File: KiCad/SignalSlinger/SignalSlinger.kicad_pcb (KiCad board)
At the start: 2 copper layers, 92.1 x 59.1 mm, 106 parts, among them J101 Conn_01x02, J102 Conn_01x03, J103 Conn_01x02, J104 Conn_01x02, J105 Conn_01x04, J106 Conn_01x02, J107 DB9 Female, J108 Conn_01x02, J109 Conn_01x03, J201 Barrel_Jack_Switch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

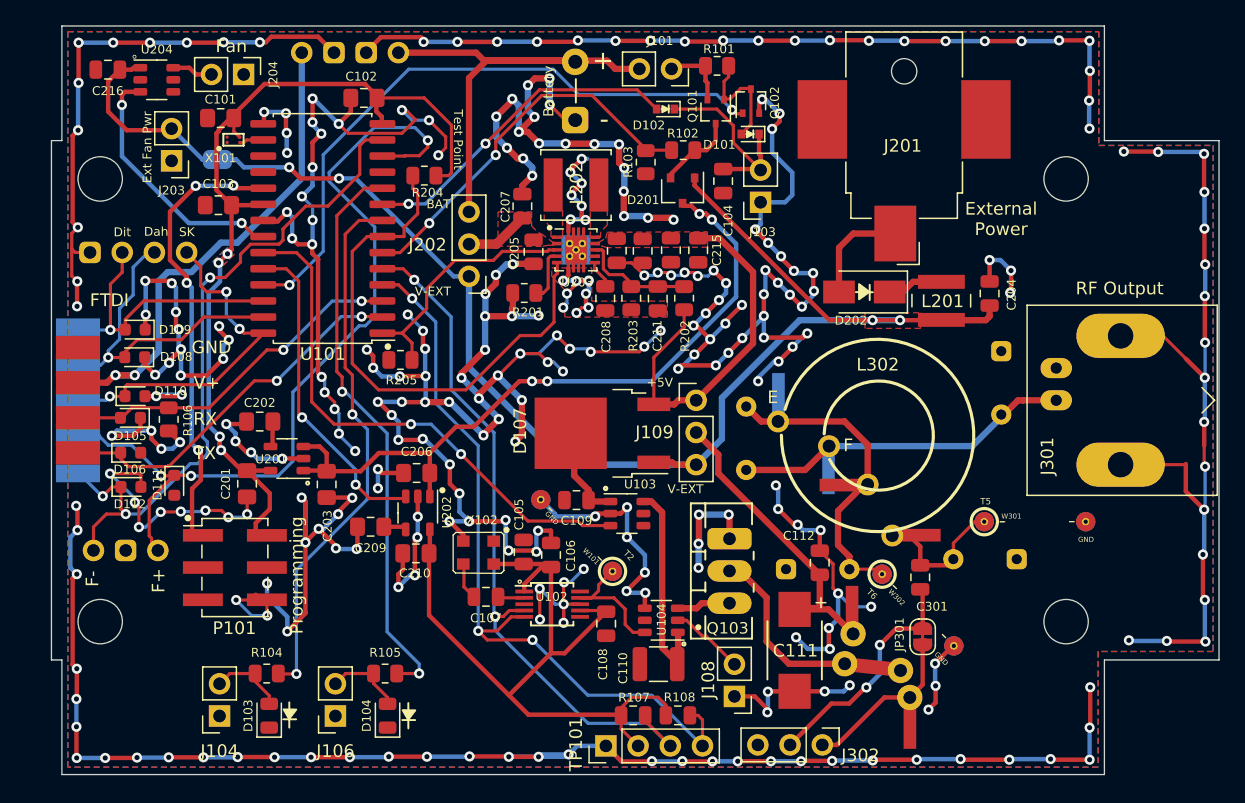
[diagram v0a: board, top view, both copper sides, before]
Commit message: Schematic Updates
o Added support for a linear adjustable voltage regulator
o Added a switch
o Re-arranged components for a better fit
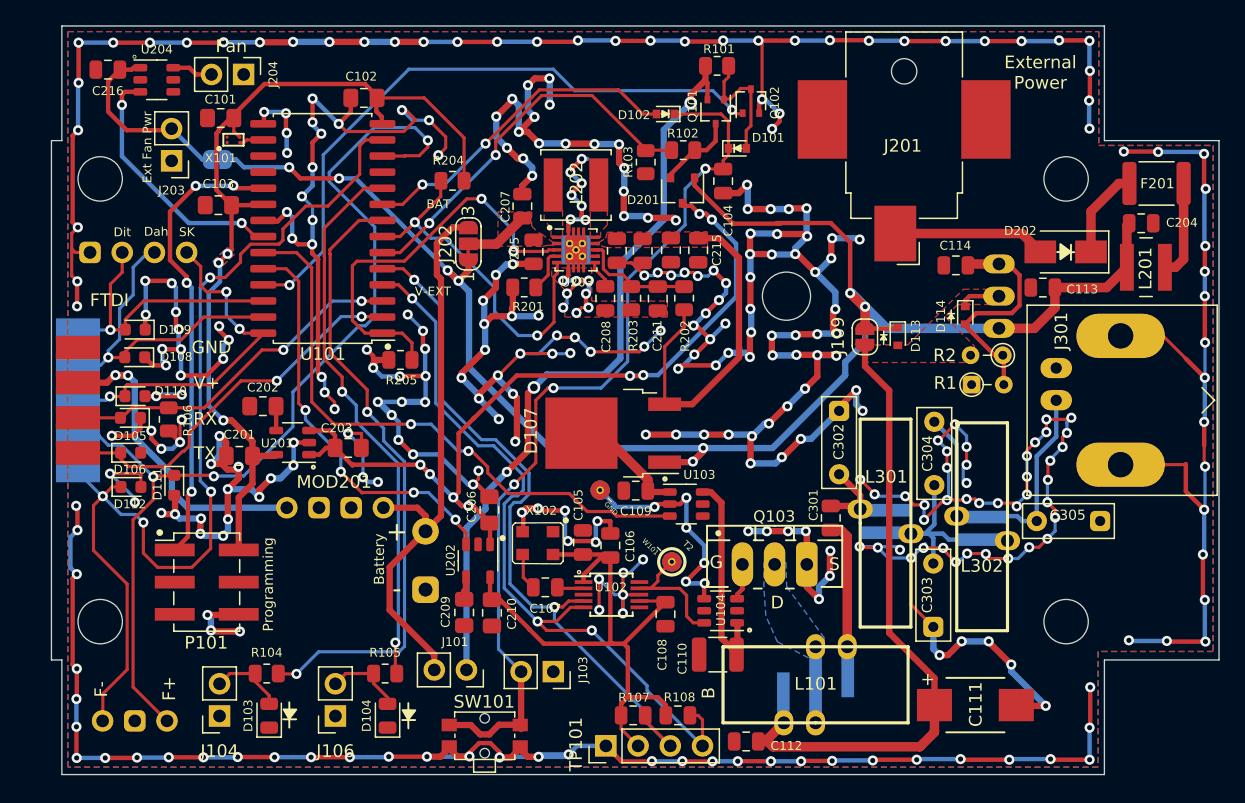
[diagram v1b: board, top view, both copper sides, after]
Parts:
- removed J108: Conn_01x02, Connector_PinHeader_2.54mm:PinHeader_1x02_P2.54mm_Vertical
- removed J302: Conn_01x03, Connector_PinHeader_2.54mm:PinHeader_1x03_P2.54mm_Vertical
- removed JP301: QRP disable, Jumper:SolderJumper-2_P1.3mm_Bridged_RoundedPad1.0x1.5mm
- removed W301: T5, Measurement:Measurement_Point_ScopeProbe_Round-SMD-2sides-Pad_Small
- removed W302: T6, Measurement:Measurement_Point_ScopeProbe_Round-SMD-2sides-Pad_Small
- added C113: 10uF, Capacitor_SMD:C_0805_2012Metric, F.Cu at (126.2, 80.5)
- added C114: 10uF, Capacitor_SMD:C_0805_2012Metric, F.Cu at (119.4, 78.8)
- added D113: 1N914WT, Diode_SMD:D_SOD-523, F.Cu at (114.8, 84.4)
- added D114: 1N914WT, Diode_SMD:D_SOD-523, F.Cu at (120.1, 82.7)
- added F201: 1.1A, Fuse:Fuse_1812_4532Metric, F.Cu at (135.2, 72.3)
- added R1: TBD, Resistor_THT:R_Axial_DIN0204_L3.6mm_D1.6mm_P2.54mm_Vertical, F.Cu at (120.6, 88.2)
- added R2: TBD, Resistor_THT:R_Axial_DIN0204_L3.6mm_D1.6mm_P2.54mm_Vertical, F.Cu at (123.1, 85.9)
- added SW101: SW_SPST, Button_Switch_SMD:SW_SPST_TL1014BF160QG, F.Cu at (82.2, 115.9)
- added U105: LT1086-ADJ, TO_SOT_Packages:TO-220_Neutral123_Horizontal, B.Cu at (122.8, 81.2)
- C302, C303, C304, C305: moved to F.Cu
- J109: value Conn_01x03 -> SolderJumper_2_Bridged; footprint Connector_PinHeader_2.54mm:PinHeader_1x03_P2.54mm_Vertical -> Jumper:SolderJumper-2_P1.3mm_Bridged_RoundedPad1.0x1.5mm
- J202: value Conn_01x03 -> SolderJumper_3_Bridged12; footprint Connector_PinHeader_2.54mm:PinHeader_1x03_P2.54mm_Vertical -> Jumper:SolderJumper-3_P1.3mm_Bridged12_RoundedPad1.0x1.5mm_NumberLabels
- L101: footprint Inductors:Toroid_T-50A_TH_BF_CT -> Inductors:Toroid_T-50A_TH_BF_CT_Vertical; moved to F.Cu
- L301: footprint Inductors:Toroid_T-60_2TH -> Inductors:Toroid_T-60_2TH_Vertical; moved to F.Cu
- L302: footprint Inductors:Toroid_T-60_2TH -> Inductors:Toroid_T-60_2TH_Vertical
- R105: value 1k -> 220
- R203: value 105k -> 80.6k
- moved J101 50.1 mm to (80.8, 110.7)
- moved J103 40.5 mm to (87.6, 110.8), turned to -90 degrees
- moved BT201 38.9 mm to (77.5, 99.8)
- moved MOD201 35.9 mm to (74.2, 97.9)
- moved L201 16.4 mm to (134.3, 78.9), turned to 180 degrees
- moved D202 16.2 mm to (128.0, 77.7)
- moved C304 15.3 mm to (117.7, 91.1), turned to -90 degrees
- moved C112 15.2 mm to (102.8, 116.3), turned to 0 degrees
- moved C111 14.9 mm to (120.9, 113.5), turned to 0 degrees
- moved J109 14.2 mm to (112.2, 84.4), turned to -90 degrees
- moved J102 13.5 mm to (52.0, 114.7)
- moved C204 13.2 mm to (134.0, 75.5), turned to 180 degrees
- moved C303 12.5 mm to (117.6, 107.3), turned to 90 degrees
- moved C302 11.2 mm to (110.2, 95.2), turned to 90 degrees
- moved L302 10.9 mm to (121.4, 99.4), turned to 180 degrees
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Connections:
- C112 pad 1: Net-(C111-Pad1) -> GND
- C112 pad 2: GND -> Net-(C111-Pad1)
- C212 pad 1: +5V -> +7V
- C213 pad 2: +5V -> +7V
- C214 pad 2: +5V -> +7V
- C215 pad 2: +5V -> +7V
- C301 pad 1: Net-(C301-Pad1) -> RF_Raw
- D107 pad 3: +5V -> +7V
- J109 pad 1: +5V -> V_ext
- L201 pad 1: Net-(D202-Pad1) -> Net-(L201-Pad1)
- R202 pad 1: +5V -> +7V
- U104 pad 2: Net-(J108-Pad2) -> unconnected-(U104-Pad2)
- U203 pad 9: +5V -> +7V
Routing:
- net GND: track 796.1 -> 863.4 mm, vias 306 -> 353
- net Net-(J101-Pad1): track 5.11 -> 59.7 mm, vias 0 -> 3
- net Net-(C104-Pad1): track 15.4 -> 69.9 mm, vias 0 -> 3
- net +5V: track 29.3 -> 0.00 mm
- net Net-(C111-Pad1): track 25.1 -> 52.6 mm
- net V_ext: track 106.9 -> 134.3 mm, vias 4 -> 8
- net +7V: track 0.00 -> 27.2 mm
- net Frequency Down: track 54.6 -> 79.6 mm, vias 3 -> 4
- net Net-(C301-Pad1): track 18.5 -> 0.00 mm, vias 2 -> 0
- net Net-(R1-Pad2): track 0.00 -> 17.0 mm
- net Power_Good: track 42.9 -> 28.4 mm, vias 0 -> 2
- net V+_Charging: track 40.6 -> 26.5 mm
- net Net-(L101-Pad2): track 13.3 -> 0.00 mm
- net Frequency Up: track 66.4 -> 79.6 mm
- net B/B_PS_Enable: track 19.6 -> 31.9 mm, vias 0 -> 2
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- added copper zone on F.Cu, net +7V
- added copper zone on F.Cu, net Net-(C111-Pad1)
- added copper zone on B.Cu, net Net-(L101-Pad2)
- removed copper zone on F.Cu, net +5V
- removed copper zone on F.Cu, net V_ext
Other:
- board text added: "SignalSlinger github.com/OpenARDF/SignalSlinger Open Source: MIT License Model: SS-80/40 Nov 2023"
- board text removed: "+5V"
- board text removed: "Adafruit LiIon Charging Module PID_1904"
- board text removed: "Foxoring Module"
- board text removed: "SignalSlinger github.com/OpenARDF/SignalSlinger Open Source: MIT License Model: SS-80/40 July 2023"
- board text removed: "Test Point"

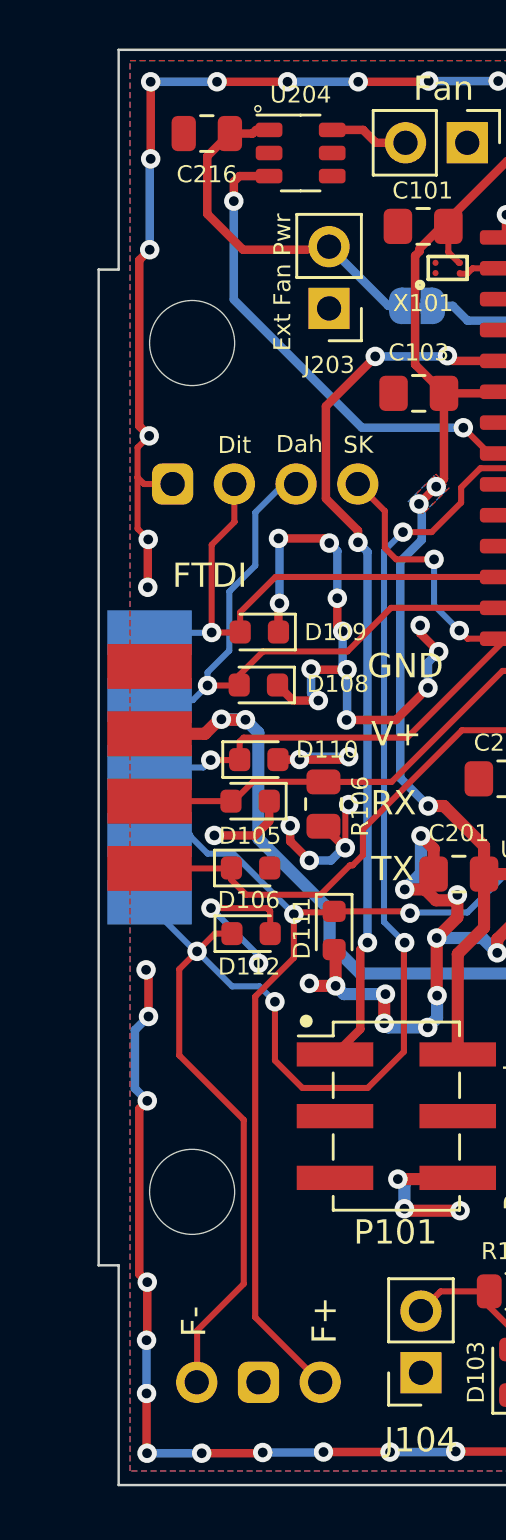
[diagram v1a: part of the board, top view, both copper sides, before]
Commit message: PCB Updates
Moved DB9 2mm farther left, and extended PCB to match.
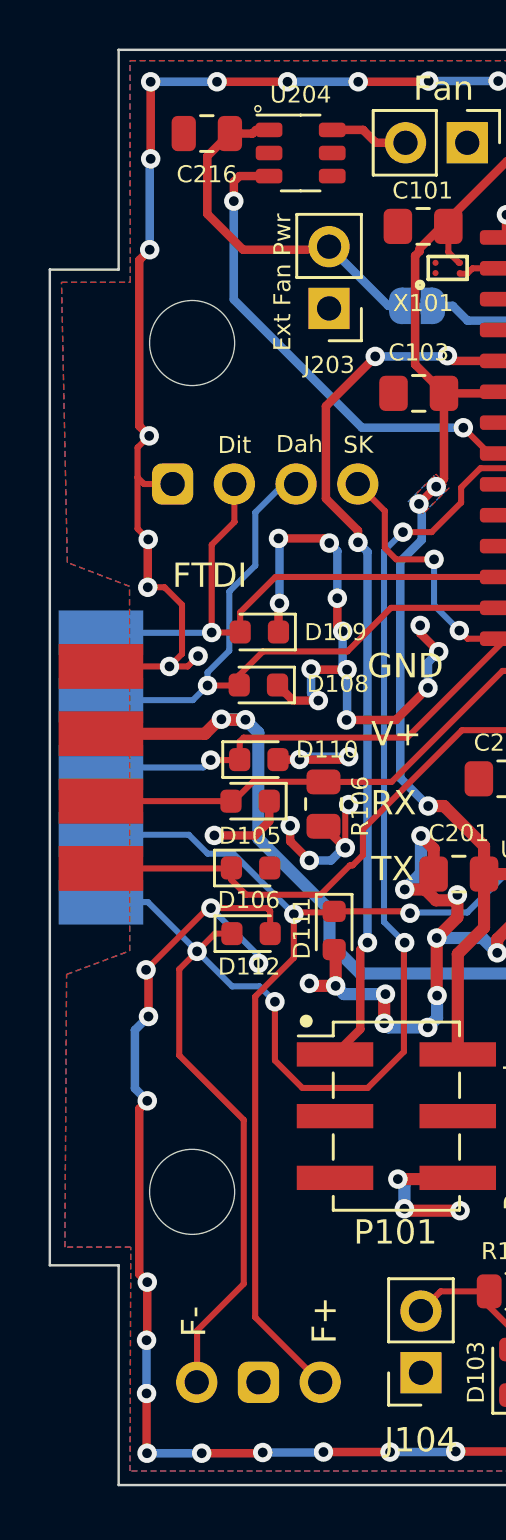
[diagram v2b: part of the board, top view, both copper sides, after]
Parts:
- moved J107 2.00 mm to (48.1, 89.4)
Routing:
- net GND: track 863.4 -> 875.7 mm, vias 353 -> 355
- net Frequency Down: track 79.6 -> 81.7 mm
- net Frequency Up: track 79.6 -> 81.6 mm
- net V+_Charging: track 26.5 -> 28.4 mm
- net Straightkey: track 27.8 -> 29.7 mm
- net Paddle_Dit: track 22.4 -> 24.3 mm
- net Paddle Dah: track 26.0 -> 27.9 mm
- net Net-(D106-Pad1): track 30.1 -> 32.0 mm
- net Net-(D105-Pad2): track 27.8 -> 29.7 mm
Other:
- board size 92.1 x 59.1 mm -> 94.1 x 59.1 mm

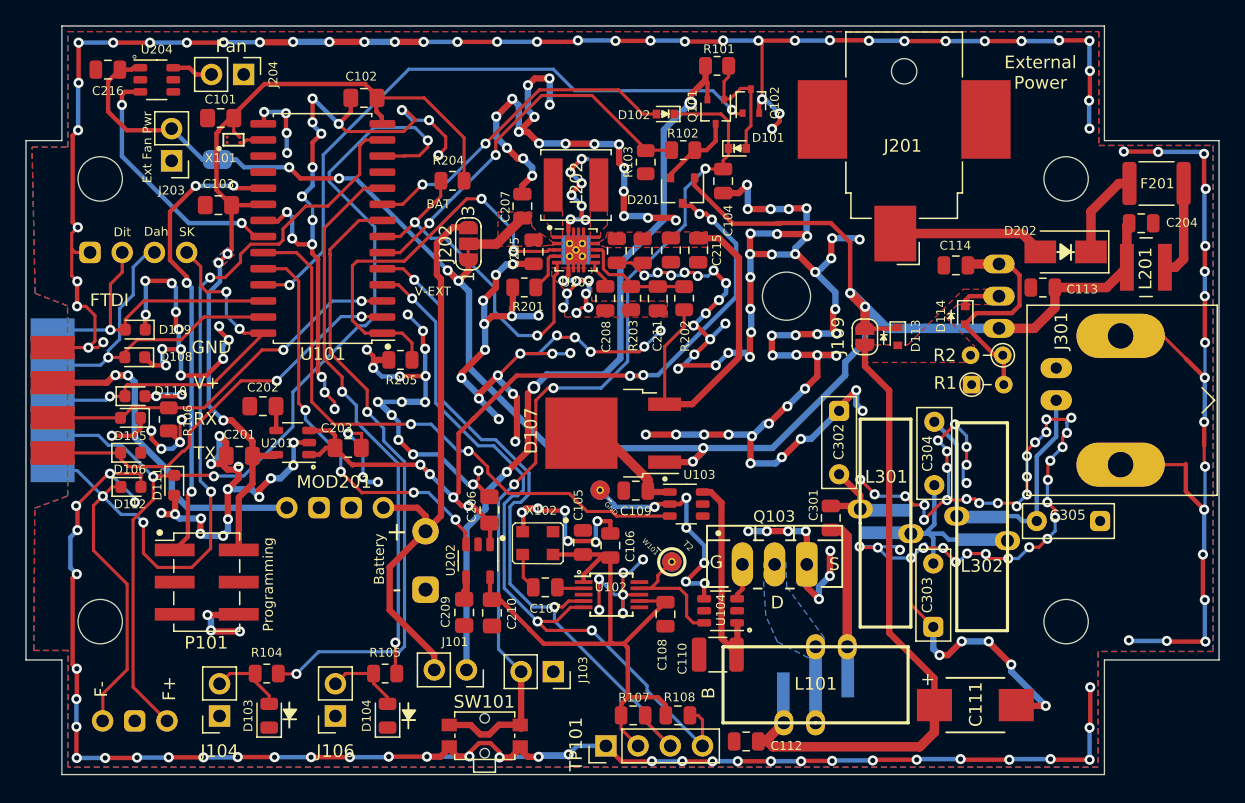
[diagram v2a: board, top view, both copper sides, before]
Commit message: DB9 Pinout Updates
o Updated schematic (Rev 2.0)
o Updated PCB
o Updated Gerbers
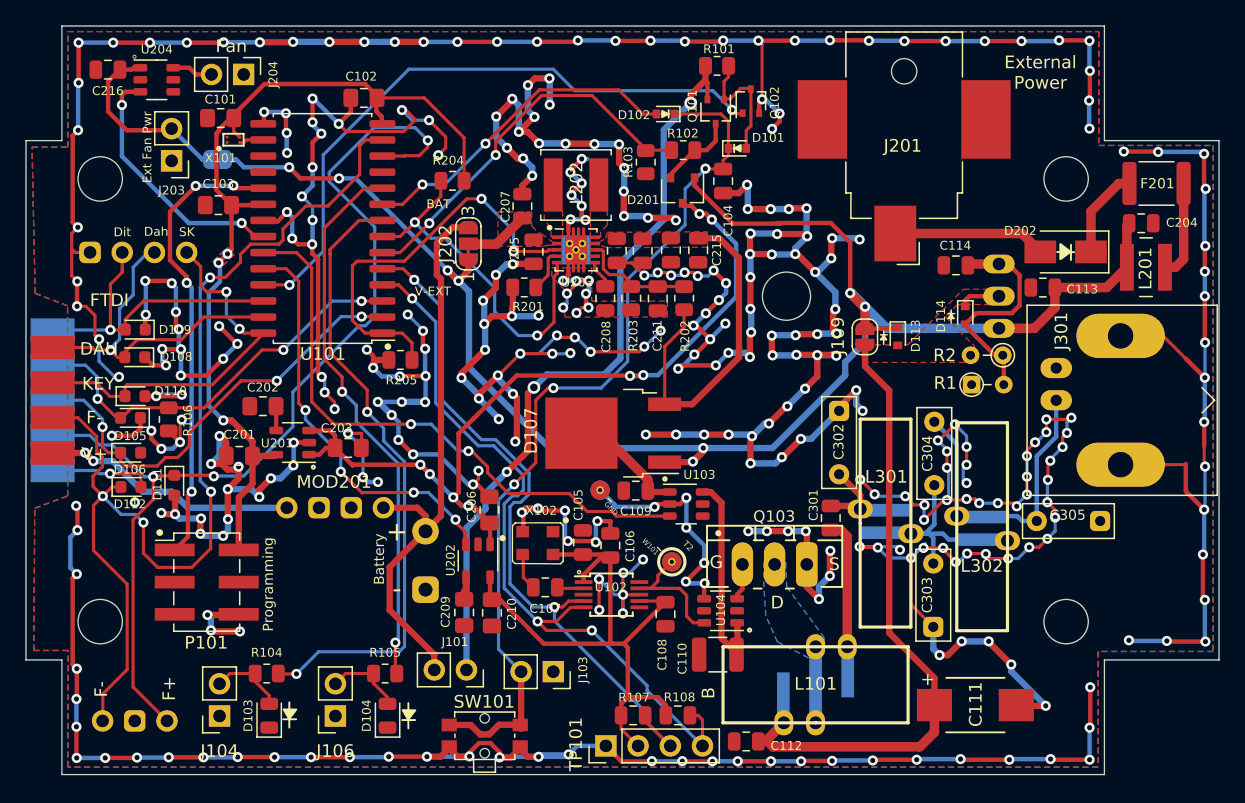
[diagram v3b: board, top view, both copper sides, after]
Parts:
- U105: value LT1086-ADJ -> TO-220 ADJ Reg.
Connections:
- D105 pad 2: Net-(D105-Pad2) -> Net-(J107-Pad2)
- D106 pad 1: Net-(D106-Pad1) -> Net-(J107-Pad3)
- J107 pad 2: Paddle Dah -> Net-(J107-Pad2)
- J107 pad 3: Straightkey -> Net-(J107-Pad3)
- J107 pad 5: Frequency Down -> GND
- J107 pad 6: GND -> Paddle Dah
- J107 pad 7: V+_Charging -> Straightkey
- J107 pad 8: Net-(D105-Pad2) -> Frequency Down
- J107 pad 9: Net-(D106-Pad1) -> V+_Charging
- R106 pad 1: Net-(D105-Pad2) -> Net-(J107-Pad2)
- U101 pad 2: Net-(D106-Pad1) -> Net-(J107-Pad3)
- U101 pad 3: Net-(D105-Pad2) -> Net-(J107-Pad2)
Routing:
- net Net-(J107-Pad3): track 0.00 -> 35.3 mm, vias 0 -> 3
- net Net-(J107-Pad2): track 0.00 -> 32.4 mm, vias 0 -> 3
- net Net-(D106-Pad1): track 32.0 -> 0.00 mm, vias 2 -> 0
- net Net-(D105-Pad2): track 29.7 -> 0.00 mm, vias 2 -> 0
- net V+_Charging: track 28.4 -> 21.2 mm
- net Frequency Down: track 81.7 -> 86.5 mm
- net GND: track 875.7 -> 873.4 mm
- net Paddle Dah: track 27.9 -> 27.3 mm
- net Straightkey: track 29.7 -> 30.0 mm, vias 3 -> 2
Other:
- board text added: "RXD"
- board text added: "SignalSlinger github.com/OpenARDF/SignalSlinger Open Source: MIT License Model: SS-80 Nov 2023"
- board text added: "TXD"
- board text removed: "FREQ+"
- board text removed: "FREQ-"
- board text removed: "RX"
- board text removed: "SignalSlinger github.com/OpenARDF/SignalSlinger Open Source: MIT License Model: SS-80/40 Nov 2023"
- board text removed: "TX"

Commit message: Updates
PCB and FreeCAD file updates. PCB layout improved to ensure all parts fit without interference.
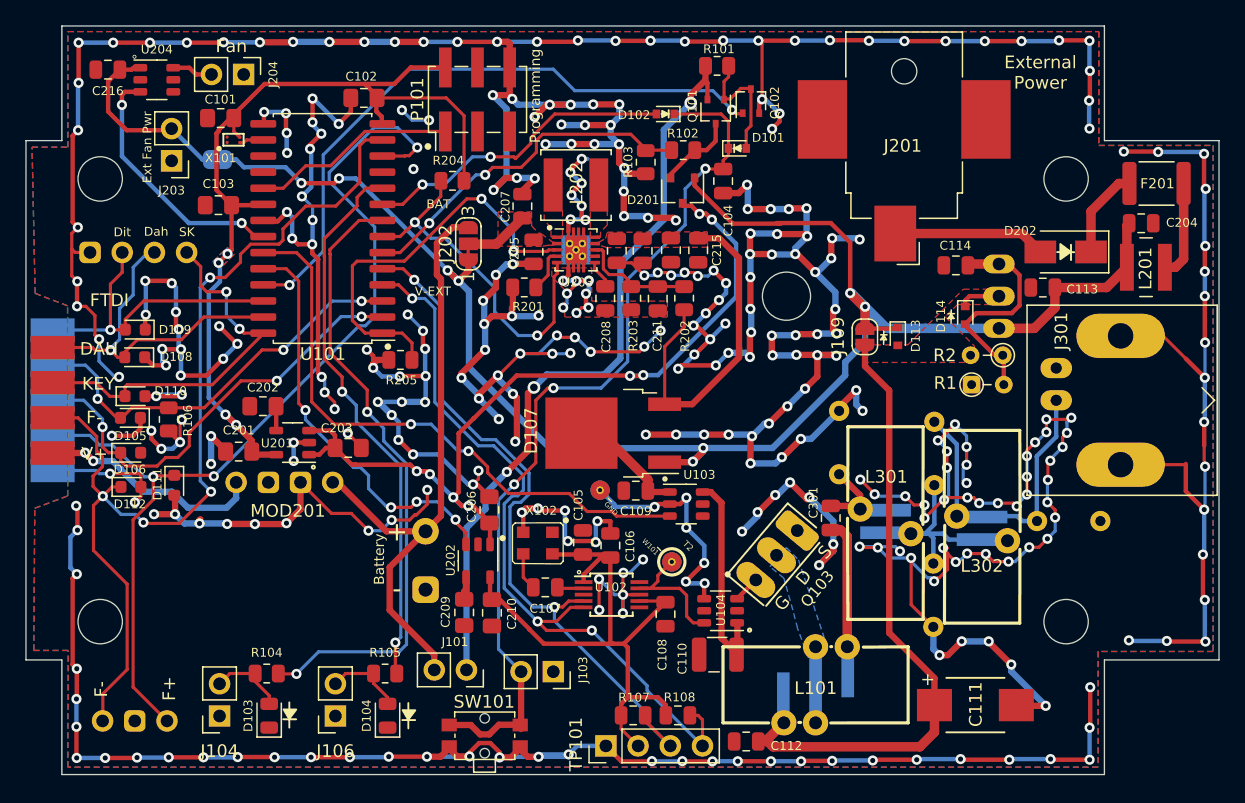
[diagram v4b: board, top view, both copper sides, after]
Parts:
- C302, C303, C304, C305: moved to B.Cu
- moved P101 43.7 mm to (81.6, 65.7), turned to 90 degrees
- moved MOD201 4.47 mm to (70.2, 95.9)
- moved Q103 0.74 mm to (105.2, 101.6), turned to 50 degrees
- moved C201 0.34 mm to (62.8, 93.5)
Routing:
- net Net-(P101-Pad1): track 36.3 -> 16.2 mm, vias 4 -> 0
- net GND: track 873.4 -> 880.8 mm, vias 355 -> 352
- net Frequency Down: track 86.5 -> 79.9 mm
- net +BATT: track 44.7 -> 48.9 mm
- net Frequency Up: track 81.6 -> 78.2 mm
- net Vbat: track 30.4 -> 27.8 mm
- net V+_Charging: track 21.2 -> 18.8 mm
- net Net-(D102-Pad2): track 26.2 -> 25.0 mm
- net Net-(Q103-Pad1): track 2.88 -> 2.10 mm
- net +3V3: track 71.0 -> 71.6 mm, vias 3 -> 4
- net Net-(R108-Pad1): track 59.2 -> 59.8 mm
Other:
- board text removed: "D"
- board text removed: "G"
- board text removed: "S"

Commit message: KiCad Updates
Updated schematic and PCB.
Added diodes to support USB powering the processor and replacing J202
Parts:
- removed J202: SolderJumper_3_Bridged12, Jumper:SolderJumper-3_P1.3mm_Bridged12_RoundedPad1.0x1.5mm_NumberLabels
- added D203: Schottky Diode, Diode_SMD:D_SOD-123, F.Cu at (65.1, 99.8)
- added D204: Schottky Diode, Diode_SMD:D_SOD-123, F.Cu at (80.3, 79.8)
- D113, D114: value 1N914WT -> 1N4001; footprint Diode_SMD:D_SOD-523 -> Diode_SMD:D_SOD-123F
- J203: value External Power Source -> External Fan Power
- moved JP201 0.67 mm to (61.1, 71.1)
- moved D114 0.66 mm to (119.5, 82.5)
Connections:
- C205 pad 2: Net-(C205-Pad2) -> V_ext
- C207 pad 2: Net-(C205-Pad2) -> V_ext
- U203 pad 2: Net-(C205-Pad2) -> V_ext
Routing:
- net Net-(C203-Pad2): track 67.9 -> 77.2 mm
- net +BATT: track 48.9 -> 41.9 mm
- net V_ext: track 134.6 -> 140.1 mm
- net Net-(C205-Pad2): track 5.06 -> 0.00 mm
- net V+_Charging: track 18.8 -> 23.1 mm
- net GND: track 880.8 -> 883.3 mm
- net Net-(C114-Pad1): track 17.0 -> 18.3 mm
- net Net-(C216-Pad1): track 14.2 -> 15.1 mm
- added copper zone on F.Cu, net V_ext
- removed copper zone on F.Cu, net Net-(C205-Pad2)
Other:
- board text added: "X"
- board text added: "Y"
- board text removed: "V-EXT"
